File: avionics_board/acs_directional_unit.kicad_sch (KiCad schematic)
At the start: 7 parts, among them J8 Conn_01x04, U13 INA226, U14 DRV8838

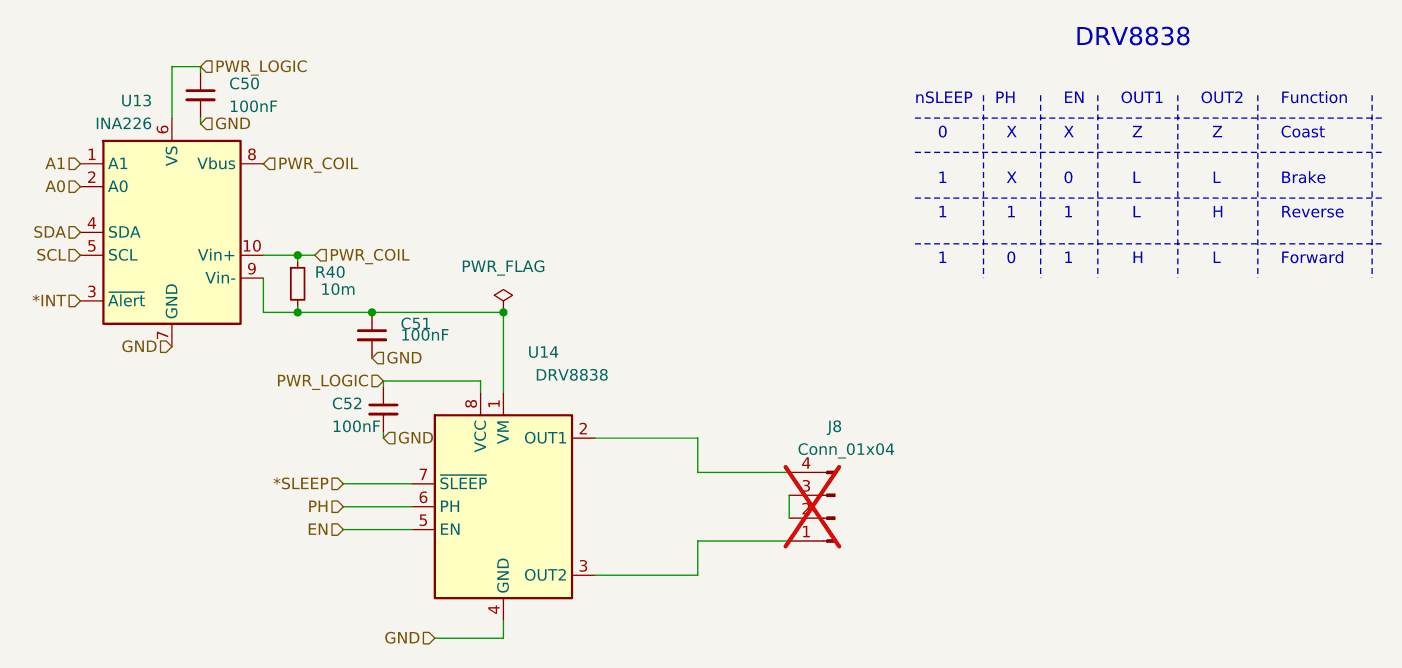
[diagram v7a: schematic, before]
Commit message: use small connectors in corners and on sides for sun sensors and solar cells
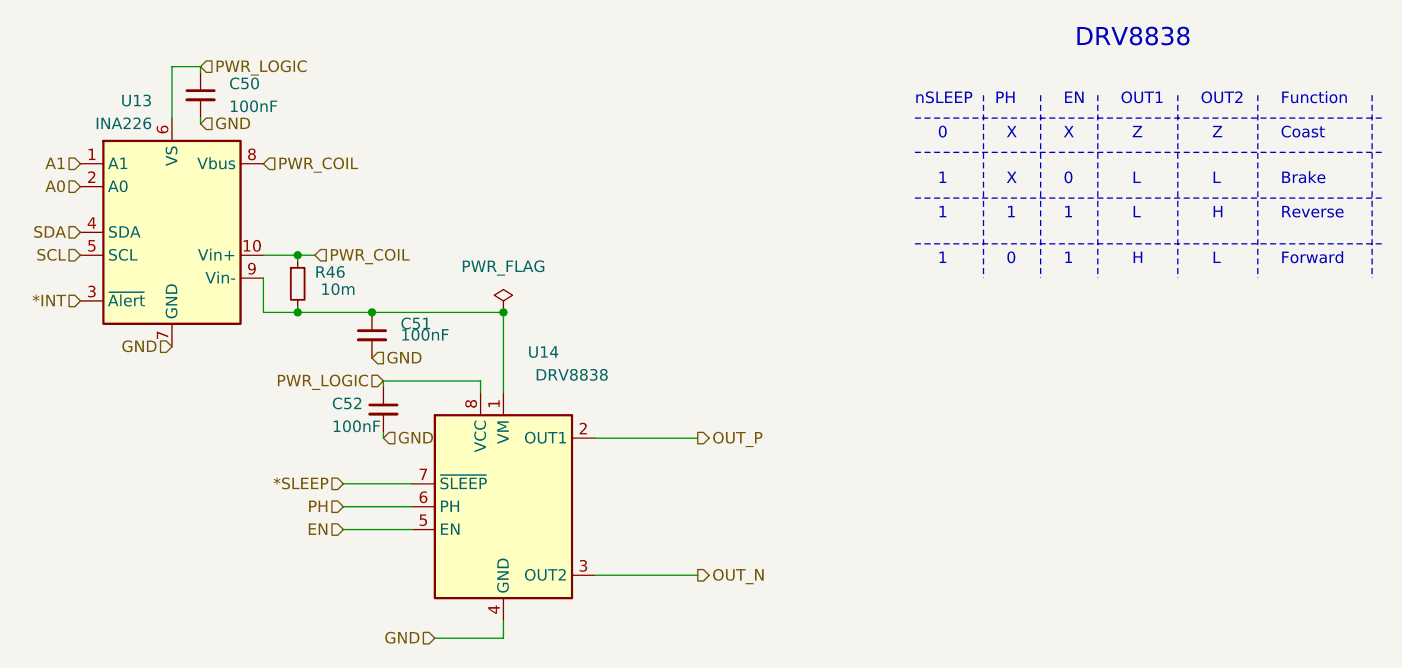
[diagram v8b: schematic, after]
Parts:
- removed J8: Conn_01x04, Connector_PinHeader_2.54mm:PinHeader_1x04_P2.54mm_Vertical, symbol Connector:Conn_01x04_Pin
- U14: Order https://www.digikey.com/product-detail/en/texas-instruments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 -> (none)
- renumbered R40 to R46
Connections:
- net OUT_P: now reaches U14.2 (OUT1)
- net OUT_N: now reaches U14.3 (OUT2)
